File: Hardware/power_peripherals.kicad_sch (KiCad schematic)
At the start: 36 parts, among them J2 JST_2mm_LiPo, J3 Qwiic_RA, J7 Conn_01x12, J8 Conn_01x12, U5 LM66200, U6 RT9080-3.3, U7 MCP73831, U8 MAX17048, U9 RT9080-3.3

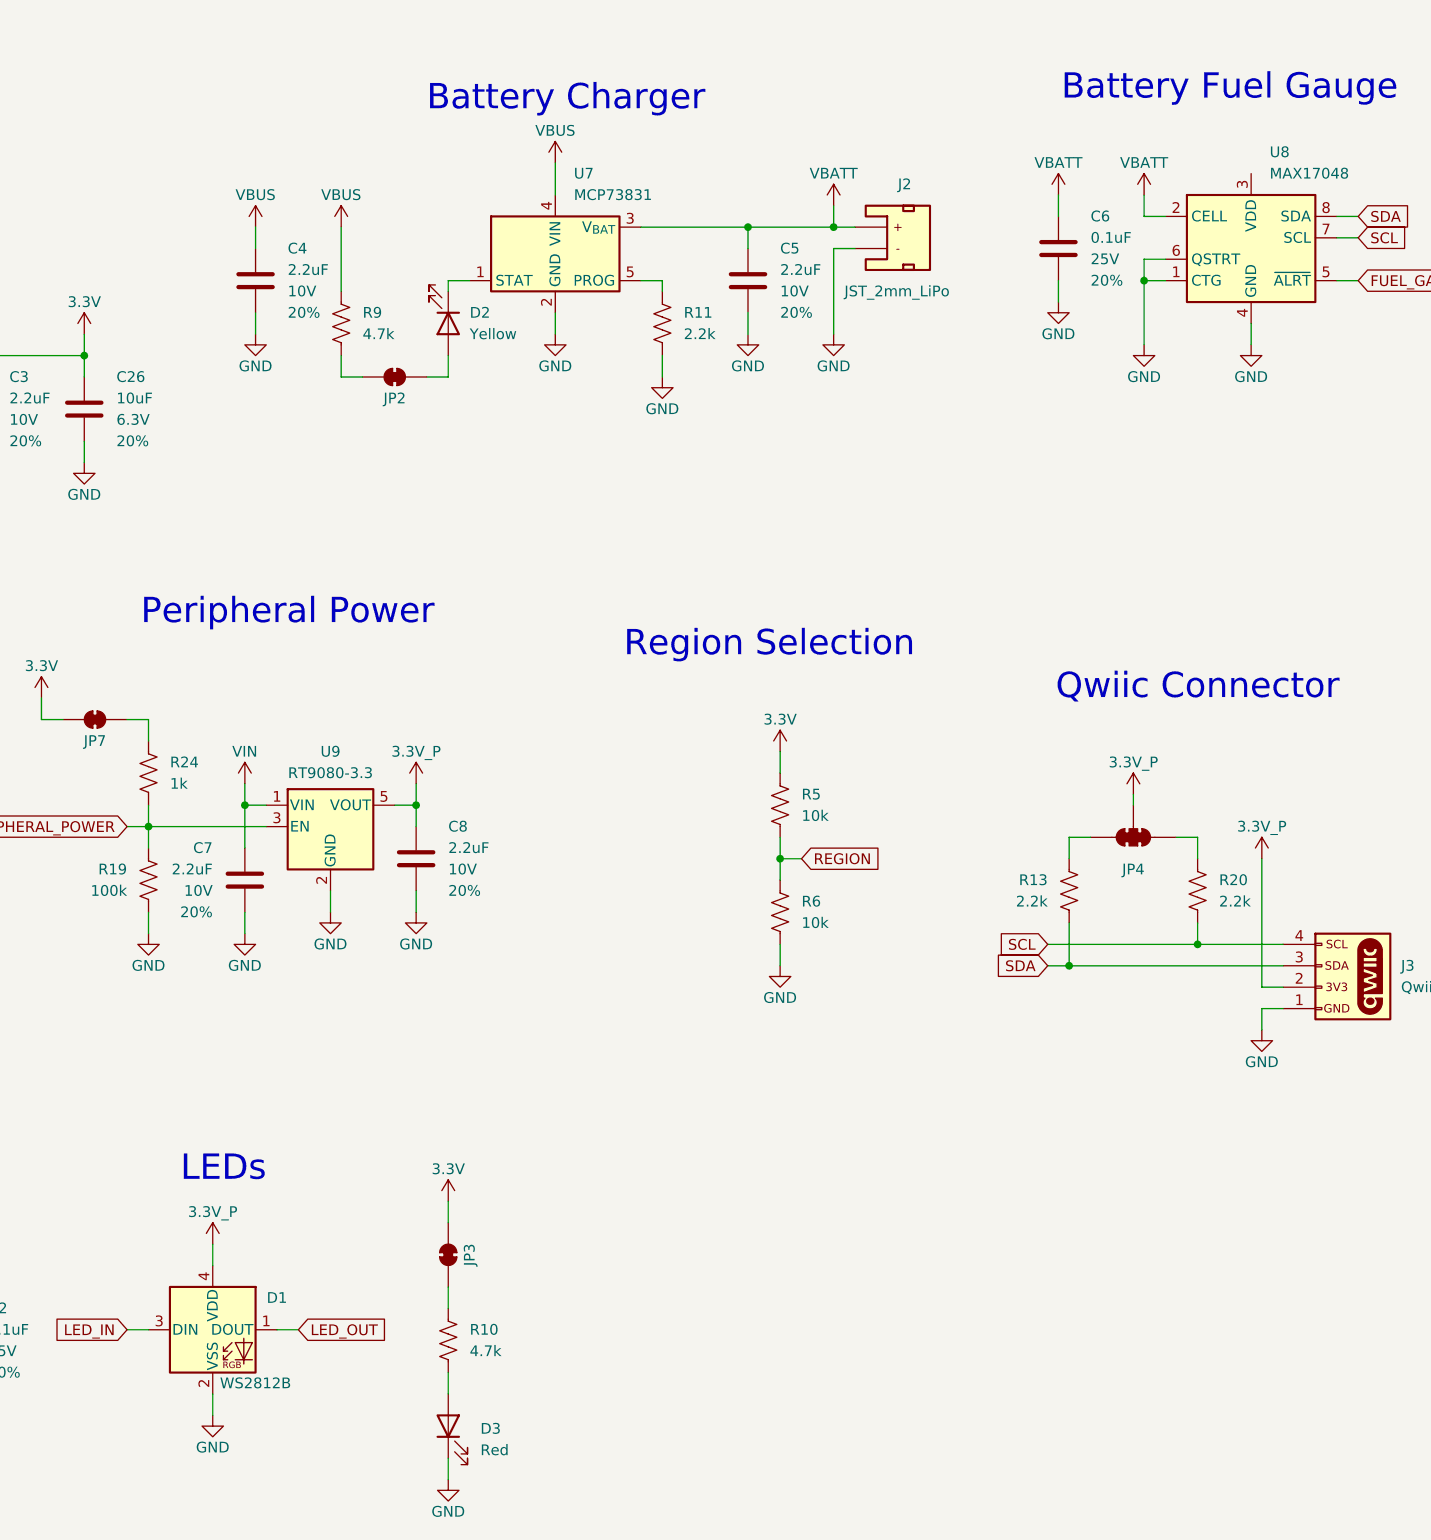
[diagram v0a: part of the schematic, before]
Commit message: Initial board layout
Board outline determined based off selected enclosure
Clusters of components placed and routed
Waiting for feedback before finishing routing
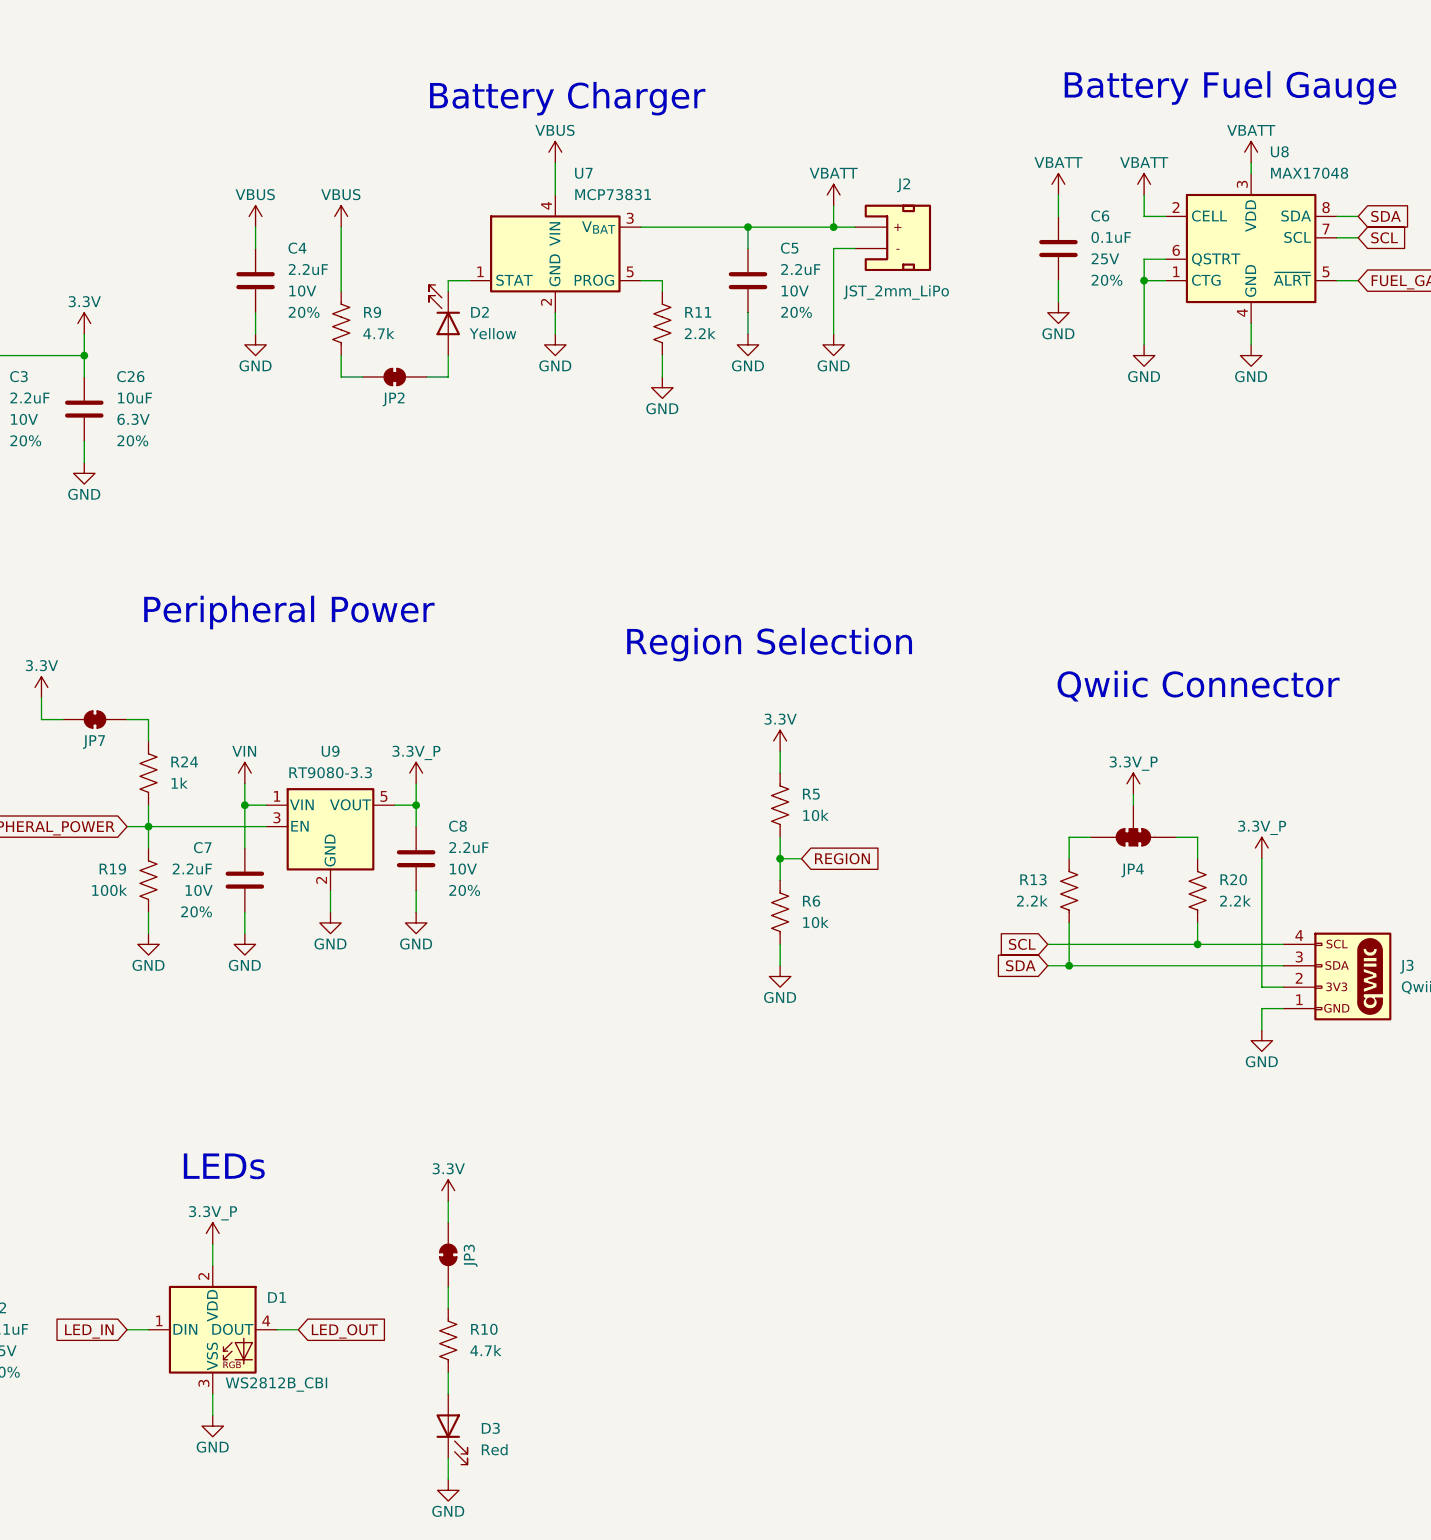
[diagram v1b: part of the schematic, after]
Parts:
- removed D1: WS2812B, SparkFun-LED:WS2812-2020, symbol SparkFun-LED:WS2812B_2020
- added D1: WS2812B_CBI, SparkFun-LED:WS2812B-CBI, symbol SparkFun-LED:WS2812B_CBI
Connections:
- net 3.3V_P: now also D1.2 (VDD)
- net GND: now also D1.3 (VSS)
- net LED_IN: now also D1.1 (DIN)
- net LED_OUT: now also D1.4 (DOUT)
- net VBATT: now also U8.3 (VDD)
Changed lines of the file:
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@@
 	(wire
 		(pts
+			(xy 247.65 33.02) (xy 247.65 34.29)
+		)
+		(stroke
+			(width 0)
+			(type default)
+		)
+	)
+	(wire
+		(pts
 			(xy 175.26 46.99) (xy 177.8 46.99)
 		)
@@
 	)
 	(symbol
+		(lib_id "SparkFun-LED:WS2812B_CBI")
+		(at 124.46 171.45 0)
+		(unit 1)
+		(exclude_from_sim no)
+		(in_bom yes)
+		(on_board yes)
+		(dnp no)
+		(fields_autoplaced yes)
+		(property "Reference" "D1"
+			(at 132.08 167.6714 0)
+			(effects
+				(font
+					(size 1.27 1.27)
+				)
+			)
+		)
+		(property "Value" "WS2812B_CBI"
+			(at 132.08 177.8 0)
+			(do_not_autoplace yes)
+			(effects
+				(font
+					(size 1.27 1.27)
+				)
+			)
+		)
+		(property "Footprint" "SparkFun-LED:WS2812B-CBI"
+			(at 110.49 180.34 0)
+			(effects
+				(font
+					(size 1.27 1.27)
+				)
+				(justify left top)
+				(hide yes)
+			)
+		)
+		(property "Datasheet" "https://cdn.sparkfun.com/datasheets/BreakoutBoards/WS2812B.pdf"
+			(at 92.71 182.245 0)
+			(effects
+				(font
+					(size 1.27 1.27)
+				)
+				(justify left top)
+				(hide yes)
+			)
+		)
+		(property "Description" "RGB LED with integrated controller"
+			(at 124.46 171.45 0)
+			(effects
+				(font
+					(size 1.27 1.27)
+				)
+				(hide yes)
+			)
+		)
+		(property "PROD_ID" "LED-20286"
+			(at 124.46 185.42 0)
+			(effects
+				(font
+					(size 1.27 1.27)
+				)
+				(hide yes)
+			)
+		)
+		(pin "2"
+		)
+		(pin "1"
+		)
+		(pin "3"
+		)
+		(pin "4"
+		)
+		(instances
+			(project ""
+				(path "/e3dd3ae4-244d-4cba-9cca-5d2abf83f29a/dbc2d9e4-ca23-4a61-9b1d-8995182ae302"
+					(reference "D1")
+					(unit 1)
+				)
+			)
+		)
+	)
+	(symbol
 		(lib_id "SparkFun-PowerSymbol:GND")
 		(at 224.79 49.53 0)
@@
 	)
 	(symbol
+		(lib_id "SparkFun-PowerSymbol:VBATT")
+		(at 247.65 33.02 0)
+		(unit 1)
+		(exclude_from_sim no)
+		(in_bom yes)
+		(on_board yes)
+		(dnp no)
+		(fields_autoplaced yes)
+		(property "Reference" "#PWR0116"
+			(at 247.65 36.83 0)
+			(effects
+				(font
+					(size 1.27 1.27)
+				)
+				(hide yes)
+			)
+		)
+		(property "Value" "VBATT"
+			(at 247.65 29.21 0)
+			(do_not_autoplace yes)
+			(effects
+				(font
+					(size 1.27 1.27)
+				)
+			)
+		)
+		(property "Footprint" ""
+			(at 247.65 33.02 0)
+			(effects
+				(font
+					(size 1.27 1.27)
+				)
+				(hide yes)
+			)
+		)
+		(property "Datasheet" ""
+			(at 247.65 33.02 0)
+			(effects
+				(font
+					(size 1.27 1.27)
+				)
+				(hide yes)
+			)
+		)
+		(property "Description" "Power symbol creates a global label with name \"VBATT\""
+			(at 247.65 33.02 0)
+			(effects
+				(font
+					(size 1.27 1.27)
+				)
+				(hide yes)
+			)
+		)
+		(pin "1"
+		)
+		(instances
+			(project "SparkFun_IoT_Node_LoRaWAN"
+				(path "/e3dd3ae4-244d-4cba-9cca-5d2abf83f29a/dbc2d9e4-ca23-4a61-9b1d-8995182ae302"
+					(reference "#PWR0116")
+					(unit 1)
+				)
+			)
+		)
+	)
+	(symbol
 		(lib_id "SparkFun-Resistor:100k_0603")
 		(at 60.96 34.29 90)
@@
 					(unit 1)
 				)
-			)
-		)
-	)
-	(symbol
-		(lib_id "SparkFun-LED:WS2812B_2020")
-		(at 124.46 171.45 0)
-		(unit 1)
-		(exclude_from_sim no)
-		(in_bom yes)
-		(on_board yes)
-		(dnp no)
-		(fields_autoplaced yes)
-		(property "Reference" "D1"
-			(at 132.08 167.6714 0)
-			(effects
-				(font
-					(size 1.27 1.27)
-				)
-			)
-		)
-		(property "Value" "WS2812B"
-			(at 129.54 177.8 0)
-			(do_not_autoplace yes)
-			(effects
-				(font
-					(size 1.27 1.27)
-				)
-			)
-		)
-		(property "Footprint" "SparkFun-LED:WS2812-2020"
-			(at 113.03 181.61 0)
-			(effects
-				(font
-					(size 1.27 1.27)
-				)
-				(justify left top)
-				(hide yes)
-			)
-		)
-		(property "Datasheet" "https://cdn.sparkfun.com/assets/e/1/0/f/b/WS2812C-2020_V1.2_EN_19112716191654.pdf"
-			(at 90.17 186.055 0)
-			(effects
-				(font
-					(size 1.27 1.27)
-				)
-				(justify left top)
-				(hide yes)
-			)
-		)
-		(property "Description" "RGB LED with integrated controller"
-			(at 124.46 171.45 0)
-			(effects
-				(font
-					(size 1.27 1.27)
-				)
-				(hide yes)
-			)
-		)
-		(property "PROD_ID" "DIO-15591"
-			(at 124.46 184.15 0)
-			(effects
-				(font
-					(size 1.27 1.27)
-				)
-				(hide yes)
-			)
-		)
-		(pin "1"
-		)
-		(pin "4"
-		)
-		(pin "2"
-		)
-		(pin "3"
-		)
-		(instances
-			(project "SparkFun_IoT_Node_LoRaWAN"
-				(path "/e3dd3ae4-244d-4cba-9cca-5d2abf83f29a/dbc2d9e4-ca23-4a61-9b1d-8995182ae302"
-					(reference "D1")
-					(unit 1)
-				)

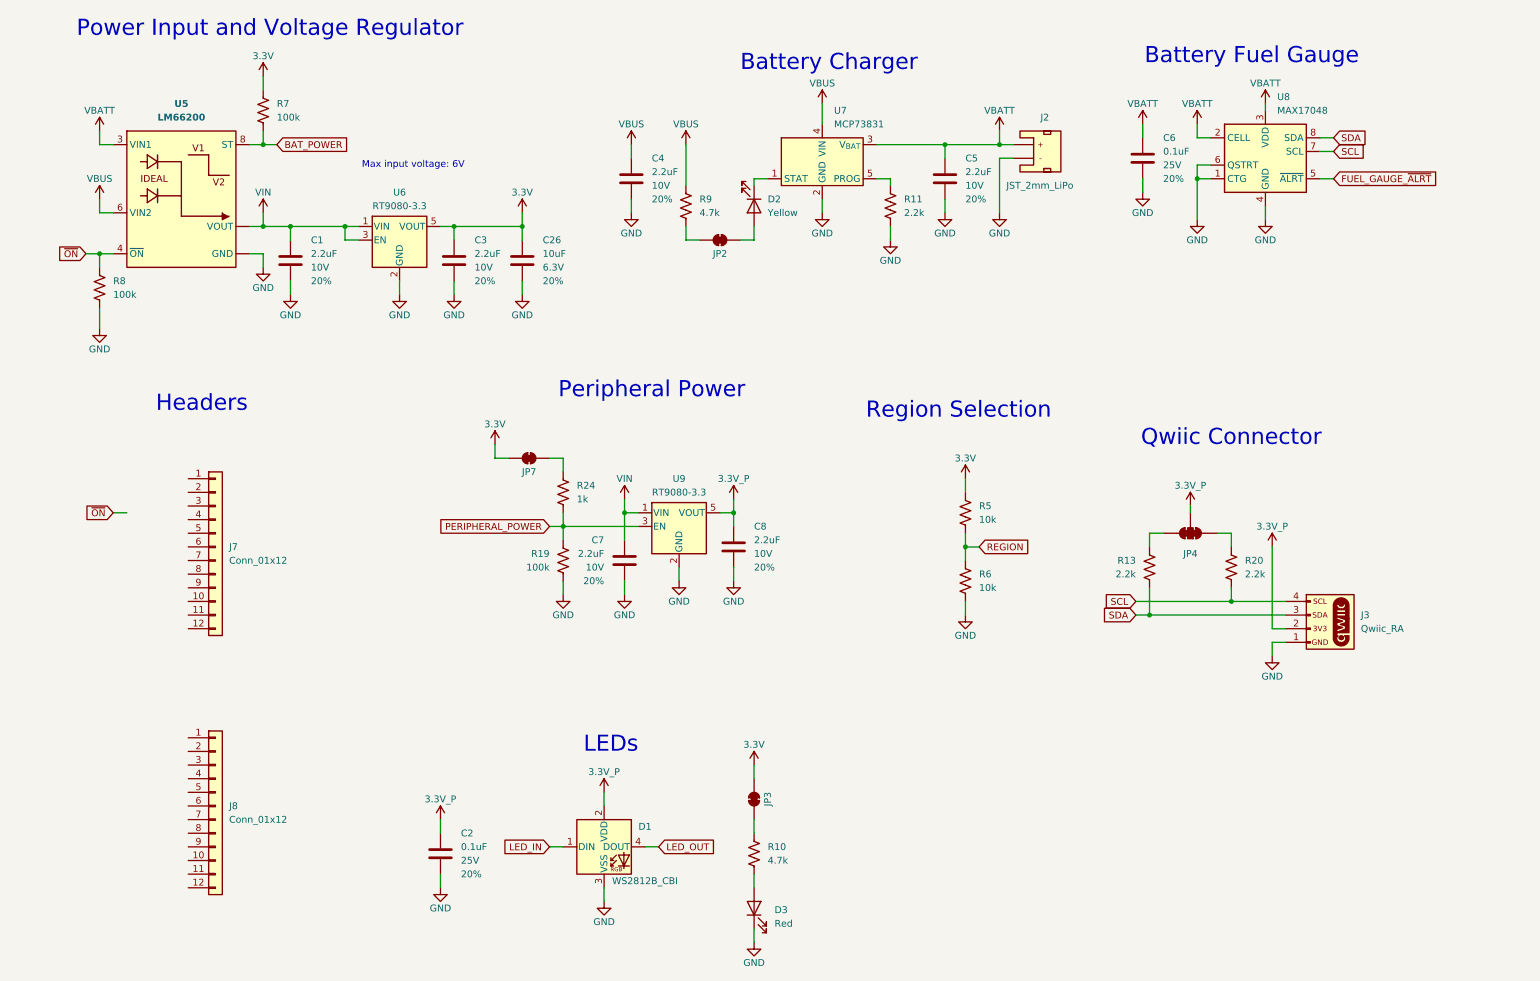
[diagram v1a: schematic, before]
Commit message: Review updates
Remove region selection resistors
Add uSD card connector
Move XBLR USB connector within enclosure
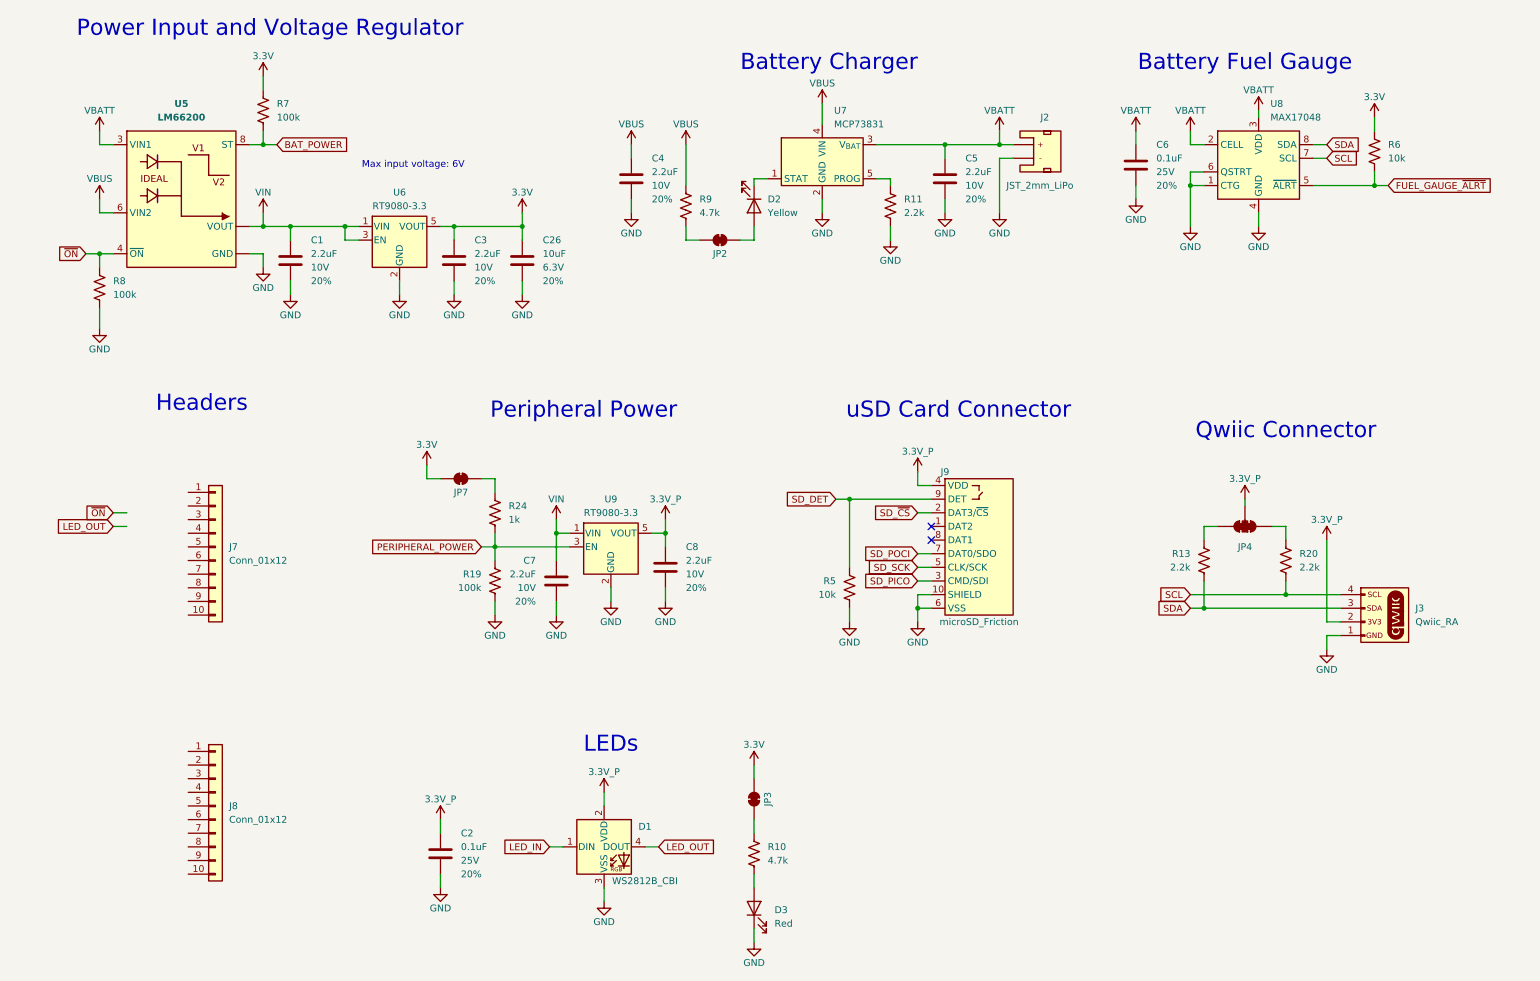
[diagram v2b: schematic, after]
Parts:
- added J9: microSD_Friction, SparkFun-Connector:microSD_Friction_Fit_Atom, symbol SparkFun-Connector:microSD_Friction
- J7, J8: footprint SparkFun-Connector:1x12 -> SparkFun-Connector:1x10; symbol SparkFun-Connector:Conn_01x12 -> SparkFun-Connector:Conn_01x10
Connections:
- net 3.3V: now also R6.1; no longer R5.1
- net 3.3V_P: now also J9.4 (VDD)
- net FUEL_GAUGE_~{ALRT}: now also R6.2
- net GND: now also R5.2, J9.10 (SHIELD), J9.6 (VSS); no longer R6.2
- removed net REGION: R5.2, R6.1
- new net SD_DET: J9.9 (DET), R5.1
- new net SD_PICO: J9.3 (CMD/SDI)
- new net SD_POCI: J9.7 (DAT0/SDO)
- new net SD_SCK: J9.5 (CLK/SCK)
- new net SD_~{CS}: J9.2 (DAT3/~{CS})
- no-connect marks 0 -> 2
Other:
- note added: "uSD Card Connector"
- note removed: "Region Selection"
- moved on the sheet: C6, C7, C8, J3, JP4, JP7, R13, R19, R20, R24, U8, U9
